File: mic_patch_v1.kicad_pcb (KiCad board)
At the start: 4 copper layers, 40 x 31 mm, 55 parts, among them J1 Conn_ARM_SWD_TagConnect_TC203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, J2 J_000002, J3 J_000001, J4 Micro_SD_Card, J5 J_000003, SW1 SW_000001, SW2 SW_000001, U1 NORA-B106-00B, U2 PWR_nPM1100-QDXX, U3 ADAU7002ACBZ-R7, Y1 CLK_0003

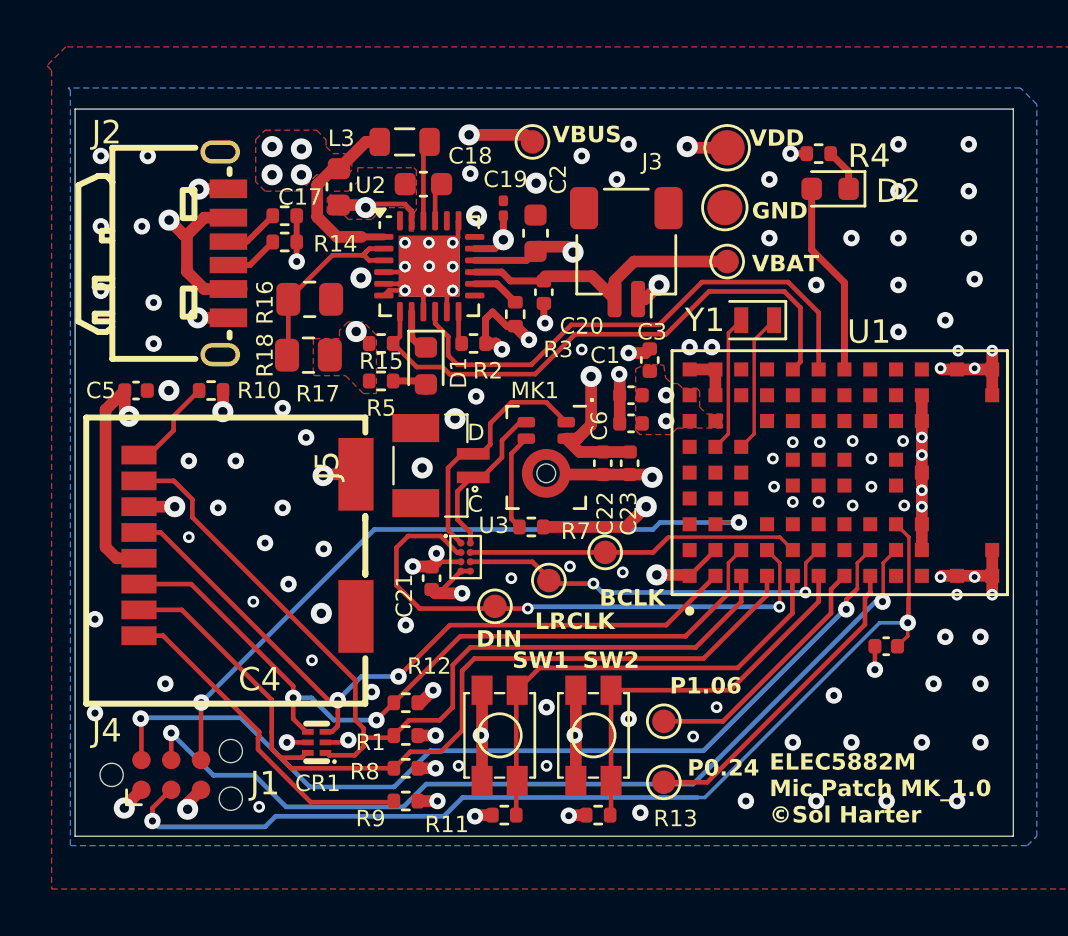
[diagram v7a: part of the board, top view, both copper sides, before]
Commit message: tidied up silkscreen
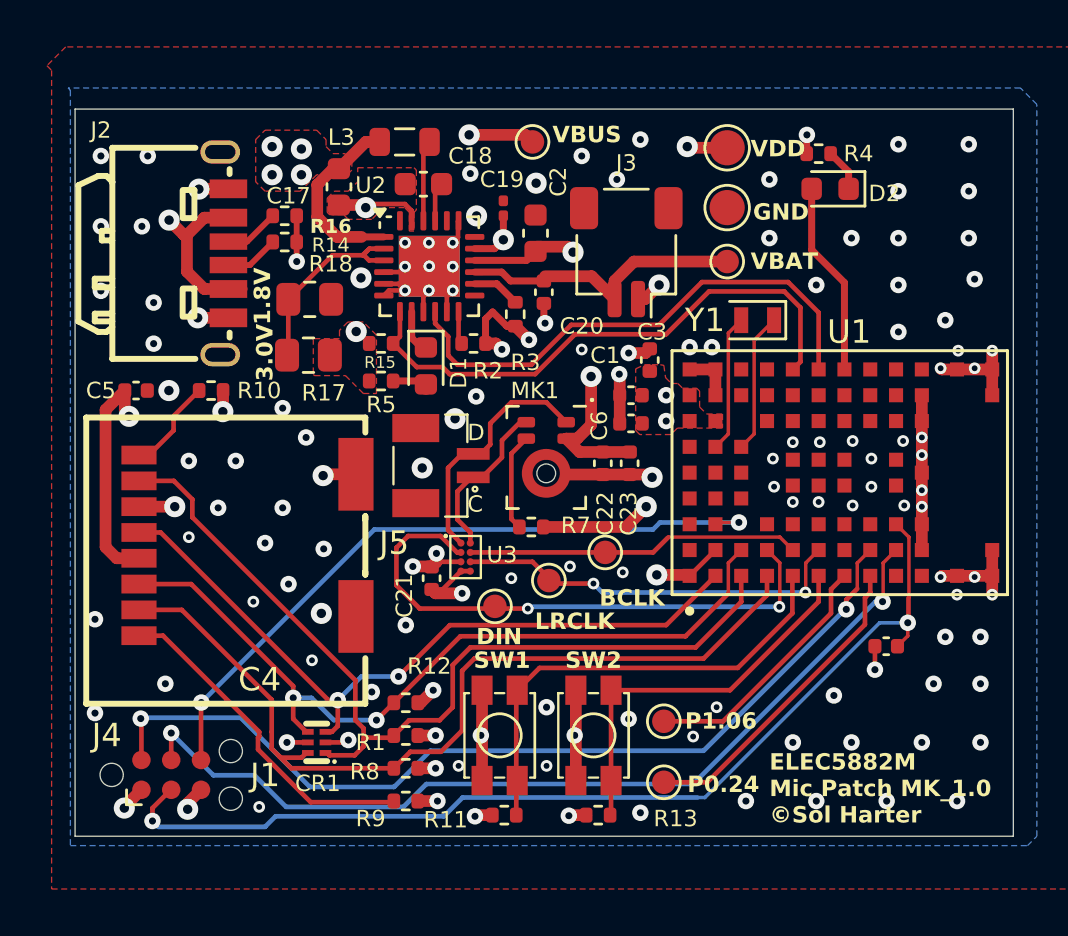
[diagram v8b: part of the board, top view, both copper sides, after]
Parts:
- moved TP2 0.10 mm to (157.7, 93.7)
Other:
- board text added: "1.8V"
- board text added: "3.0V"
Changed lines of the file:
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@@
 		(tags "capacitor")
 		(property "Reference" "C19"
-			(at 1.23 0.091 0)
+			(at 1.23 -0.059 0)
 			(layer "F.SilkS")
 			(effects
@@
 		(at 137.25 108.1 -90)
 		(property "Reference" "J4"
-			(at 7.9 6 0)
+			(at 8.1 6 0)
 			(unlocked yes)
 			(layer "F.SilkS")
@@
 		(tags "resistor")
 		(property "Reference" "R14"
-			(at 2.1628 0.084 0)
+			(at 1.9628 0.134 0)
 			(layer "F.SilkS")
 			(effects
 				(font
-					(size 0.7 0.7)
-					(thickness 0.15)
+					(size 0.6 0.6)
+					(thickness 0.1)
 				)
 			)
@@
 		(tags "LED")
 		(property "Reference" "D2"
-			(at -2.91 -0.1 180)
+			(at -2.31 -0.2 180)
 			(layer "F.SilkS")
 			(effects
 				(font
-					(size 1 1)
+					(size 0.7 0.7)
 					(thickness 0.15)
 				)
@@
 		(tags "resistor")
 		(property "Reference" "R3"
-			(at -1.503 1.833 0)
+			(at -2.053 0.433 0)
 			(layer "F.SilkS")
 			(effects
@@
 		(tags "connector JST SH horizontal")
 		(property "Reference" "J3"
-			(at -1.1 3.85 180)
+			(at 0 3.8 180)
 			(layer "F.SilkS")
 			(effects
@@
 		(tags "resistor")
 		(property "Reference" "R15"
-			(at 0 0.758 0)
+			(at -0.05 0.808 0)
 			(layer "F.SilkS")
 			(effects
 				(font
-					(size 0.7 0.7)
-					(thickness 0.15)
+					(size 0.5 0.5)
+					(thickness 0.1)
 				)
 			)
@@
 		(at 136.26375 95.65 -90)
 		(property "Reference" "J2"
-			(at -5.15 5.01375 0)
+			(at -5.25 5.26375 0)
 			(unlocked yes)
 			(layer "F.SilkS")
 			(effects
 				(font
-					(size 1 1)
+					(size 0.7 0.7)
 					(thickness 0.15)
 				)
@@
 		(tags "resistor")
 		(property "Reference" "R11"
-			(at 2.45 -0.4 180)
+			(at 2.5 -0.2 180)
 			(layer "F.SilkS")
 			(effects
@@
 		(at 152 116.2 -90)
 		(property "Reference" "SW2"
-			(at -3.2 -0.75 0)
+			(at -3.2 0 0)
 			(unlocked yes)
 			(layer "F.SilkS")
@@
 		(at 161.6 105)
 		(property "Reference" "U1"
-			(at 2.15 -6 0)
+			(at 1.3 -6 0)
 			(layer "F.SilkS")
 			(effects
@@
 		(tags "capacitor")
 		(property "Reference" "C17"
-			(at 0.433 1.65 180)
+			(at 0.383 2.15 180)
 			(layer "F.SilkS")
 			(effects
@@
 		(tags "resistor")
 		(property "Reference" "R16"
-			(at -0.8372 3.7016 90)
+			(at 1.9628 0.4516 180)
 			(layer "F.SilkS")
 			(effects
 				(font
-					(size 0.7 0.7)
-					(thickness 0.15)
+					(size 0.6 0.6)
+					(thickness 0.1)
+					(bold yes)
 				)
 			)
@@
 		(tags "resistor")
 		(property "Reference" "R18"
-			(at 1.904 -2.388 -90)
+			(at -0.896 1.512 180)
 			(layer "F.SilkS")
 			(effects
@@
 	(footprint "TestPoint:TestPoint_Pad_D1.5mm"
 		(layer "F.Cu")
-		(at 157.6 93.7)
+		(at 157.7 93.7)
 		(descr "SMD pad as test Point, diameter 1.5mm")
 		(tags "test point SMD pad")
@@
 		(tags "resistor")
 		(property "Reference" "R7"
-			(at 1.898 0.185 0)
+			(at 1.898 -0.065 0)
 			(layer "F.SilkS")
 			(effects
@@
 		(tags "inductor")
 		(property "Reference" "L3"
-			(at -2.7 -0.15 0)
+			(at -2.7 -0.2 0)
 			(layer "F.SilkS")
 			(effects
@@
 		(tags "resistor")
 		(property "Reference" "R5"
-			(at 0 1.158 0)
+			(at 0 1.008 0)
 			(layer "F.SilkS")
 			(effects
@@
 		(tags "resistor")
 		(property "Reference" "R4"
-			(at -2.15 -0.1 180)
+			(at -1.7 0 180)
 			(layer "F.SilkS")
 			(effects
 				(font
-					(size 1 1)
+					(size 0.7 0.7)
 					(thickness 0.15)
 				)
@@
 		(tags "resistor")
 		(property "Reference" "R17"
-			(at -0.4 -1.65 180)
+			(at -0.65 -1.608 0)
 			(layer "F.SilkS")
 			(effects
@@
 		(tags "tag connect programming header pogo pins")
 		(property "Reference" "J1"
-			(at 4 0.365 0)
+			(at 4 0.015 0)
 			(layer "F.SilkS")
 			(effects
@@
 		(at 145.65 104.7 90)
 		(property "Reference" "J5"
-			(at 0 -5 90)
+			(at -3.3 -2.15 0)
 			(unlocked yes)
 			(layer "F.SilkS")
@@
 				(font
 					(size 1 1)
-					(thickness 0.1)
+					(thickness 0.15)
 				)
 			)
@@
 		(tags "ADAU7002ACBZ-R7 ")
 		(property "Reference" "U3"
-			(at 1.2 -1.35 0)
+			(at 1.55 -0.1 0)
 			(unlocked yes)
 			(layer "F.SilkS")
@@
 		(tags "capacitor")
 		(property "Reference" "C2"
-			(at 2.2926 0.9694 -90)
+			(at 2.1926 0.9694 90)
 			(layer "F.SilkS")
 			(effects
@@
 		(at 148 116.2 -90)
 		(property "Reference" "SW1"
-			(at -3.2 -1.75 0)
+			(at -3.2 -0.1 0)
 			(unlocked yes)
 			(layer "F.SilkS")
@@
 	)
 	(gr_text "P0.24"
-		(at 156 118 0)
+		(at 156 118.7 0)
 		(layer "F.SilkS")
 		(effects
@@
 	)
 	(gr_text "P1.06"
-		(at 155.25 114.5 0)
+		(at 155.9 116 0)
 		(layer "F.SilkS")
 		(effects
@@
 	)
 	(gr_text "VDD"
-		(at 158.65 91.15 0)
+		(at 158.7 91.6 0)
 		(layer "F.SilkS")
 		(effects
@@
 	)
 	(gr_text "GND"
-		(at 158.75 94.25 0)
+		(at 158.8 94.3 0)
+		(layer "F.SilkS")
+		(effects
+			(font
+				(size 0.7 0.7)
+				(thickness 0.15)
+				(bold yes)
+			)
+			(justify left bottom)
+		)
+	)
+	(gr_text "1.8V"
+		(at 138.3 98.7 90)
 		(layer "F.SilkS")
 		(effects
@@
 	)
 	(gr_text "DIN"
-		(at 147 112.5 0)
+		(at 147 112.4 0)
+		(layer "F.SilkS")
+		(effects
+			(font
+				(size 0.7 0.7)
+				(thickness 0.15)
+				(bold yes)
+			)
+			(justify left bottom)
+		)
+	)
+	(gr_text "3.0V"
+		(at 138.4 101.1 90)
 		(layer "F.SilkS")
 		(effects
@@
 	)
 	(gr_text "VBAT\n"
-		(at 158.75 96.5 0)
+		(at 158.7 96.4 0)
 		(layer "F.SilkS")
 		(effects
@@
 	)
 	(segment
-		(start 161.09 91.4)
-		(end 160.4 91.4)
-		(width 0.3)
-		(layer "F.Cu")
-		(net 1)
-	)
-	(segment
 		(start 139.3472 95.9972)
 		(end 139.35 96)
@@
 	)
 	(segment
+		(start 161.09 90.61)
+		(end 161.1 90.6)
+		(width 0.3)
+		(layer "F.Cu")
+		(net 1)
+	)
+	(segment
 		(start 139.7555 116.5)
 		(end 138.932843 116.5)
@@
 	)
 	(segment
+		(start 161.09 91.4)
+		(end 161.09 90.61)
+		(width 0.3)
+		(layer "F.Cu")
+		(net 1)
+	)
+	(segment
 		(start 149.8862 98.5772)
 		(end 149.937 98.628)
@@
 	)
 	(via
-		(at 160.4 91.4)
+		(at 161.1 90.6)
 		(size 0.7)
 		(drill 0.3)
@@
 	)
 	(via
-		(at 153.5 91)
+		(at 154 90.8)
 		(size 0.7)
 		(drill 0.3)
